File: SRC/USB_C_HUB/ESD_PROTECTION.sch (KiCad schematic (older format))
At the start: 3 parts

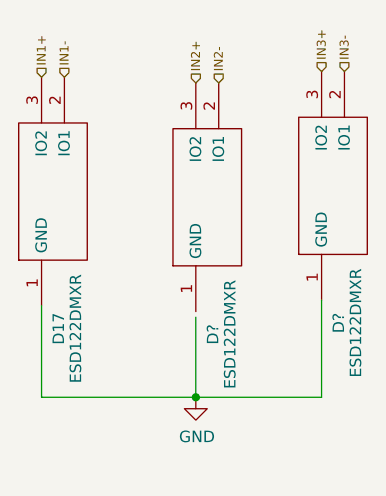
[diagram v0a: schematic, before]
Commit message: schematic capture complete. Pending Footprint assignment. accetable Errors=21
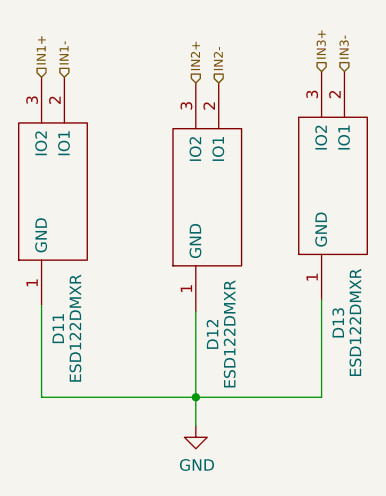
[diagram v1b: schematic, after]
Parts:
- gave numbers to parts that had none: 2
- renumbered D17 to D11
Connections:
- wire segments 5 -> 6
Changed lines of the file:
@@
 $Descr A4 11693 8268
 encoding utf-8
-Sheet 9 15
+Sheet 5 15
 Title ""
 Date ""
@@
 P 4275 4300
 AR Path="/62E89C00" Ref="D?"  Part="1"
-AR Path="/62E5065E/62E89C00" Ref="D17"  Part="1"
+AR Path="/62E5065E/62E89C00" Ref="D11"  Part="1"
 AR Path="/6317BD10/62E89C00" Ref="D20"  Part="1"
-AR Path="/63404DD9/62E89C00" Ref="D18"  Part="1"
-AR Path="/639E17BA/62E89C00" Ref="D19"  Part="1"
-F 0 "D17" H 4175 4225 50  0000 C CNN
+AR Path="/63404DD9/62E89C00" Ref="D14"  Part="1"
+AR Path="/639E17BA/62E89C00" Ref="D17"  Part="1"
+F 0 "D11" H 4175 4225 50  0000 C CNN
 F 1 "ESD122DMXR" H 4175 4150 50  0000 C CNN
 F 2 "SamacSys_Parts_2:DMX0003A" H 5125 4400 50  0001 L CNN
@@
 IN1-
 $Comp
-L OLIMEX_Power:GND #PWR0200
+L OLIMEX_Power:GND #PWR073
 U 1 1 630FD5DF
-P 4950 4700
-AR Path="/62E5065E/630FD5DF" Ref="#PWR0200"  Part="1"
-AR Path="/6317BD10/630FD5DF" Ref="#PWR0203"  Part="1"
-AR Path="/63404DD9/630FD5DF" Ref="#PWR0201"  Part="1"
-AR Path="/639E17BA/630FD5DF" Ref="#PWR0202"  Part="1"
-F 0 "#PWR0200" H 4950 4450 50  0001 C CNN
-F 1 "GND" H 4955 4527 50  0000 C CNN
-F 2 "" H 4950 4700 60  0000 C CNN
-F 3 "" H 4950 4700 60  0000 C CNN
-	1    4950 4700
+P 4950 4825
+AR Path="/62E5065E/630FD5DF" Ref="#PWR073"  Part="1"
+AR Path="/6317BD10/630FD5DF" Ref="#PWR076"  Part="1"
+AR Path="/63404DD9/630FD5DF" Ref="#PWR074"  Part="1"
+AR Path="/639E17BA/630FD5DF" Ref="#PWR075"  Part="1"
+F 0 "#PWR073" H 4950 4575 50  0001 C CNN
+F 1 "GND" H 4955 4652 50  0000 C CNN
+F 2 "" H 4950 4825 60  0000 C CNN
+F 3 "" H 4950 4825 60  0000 C CNN
+	1    4950 4825
 	1    0    0    -1
 $EndComp
@@
 P 4950 4325
 AR Path="/642DE3EE" Ref="D?"  Part="1"
-AR Path="/62E5065E/642DE3EE" Ref="D?"  Part="1"
-AR Path="/6317BD10/642DE3EE" Ref="D?"  Part="1"
-AR Path="/63404DD9/642DE3EE" Ref="D?"  Part="1"
-AR Path="/639E17BA/642DE3EE" Ref="D?"  Part="1"
-F 0 "D?" H 4850 4250 50  0000 C CNN
+AR Path="/62E5065E/642DE3EE" Ref="D12"  Part="1"
+AR Path="/6317BD10/642DE3EE" Ref="D21"  Part="1"
+AR Path="/63404DD9/642DE3EE" Ref="D15"  Part="1"
+AR Path="/639E17BA/642DE3EE" Ref="D18"  Part="1"
+F 0 "D12" H 4850 4250 50  0000 C CNN
 F 1 "ESD122DMXR" H 4850 4175 50  0000 C CNN
 F 2 "SamacSys_Parts_2:DMX0003A" H 5800 4425 50  0001 L CNN
@@
 P 5500 4275
 AR Path="/642DE7EE" Ref="D?"  Part="1"
-AR Path="/62E5065E/642DE7EE" Ref="D?"  Part="1"
-AR Path="/6317BD10/642DE7EE" Ref="D?"  Part="1"
-AR Path="/63404DD9/642DE7EE" Ref="D?"  Part="1"
-AR Path="/639E17BA/642DE7EE" Ref="D?"  Part="1"
-F 0 "D?" H 5400 4200 50  0000 C CNN
+AR Path="/62E5065E/642DE7EE" Ref="D13"  Part="1"
+AR Path="/6317BD10/642DE7EE" Ref="D22"  Part="1"
+AR Path="/63404DD9/642DE7EE" Ref="D16"  Part="1"
+AR Path="/639E17BA/642DE7EE" Ref="D19"  Part="1"
+F 0 "D13" H 5400 4200 50  0000 C CNN
 F 1 "ESD122DMXR" H 5400 4125 50  0000 C CNN
 F 2 "SamacSys_Parts_2:DMX0003A" H 6350 4375 50  0001 L CNN
@@
 Wire Wire Line
 	4275 4700 4950 4700
+Wire Wire Line
+	4950 4325 4950 4700
 Connection ~ 4950 4700
 Wire Wire Line
 	4950 4700 5500 4700
 Wire Wire Line
-	4950 4350 4950 4700
+	4950 4825 4950 4700
 $EndSCHEMATC

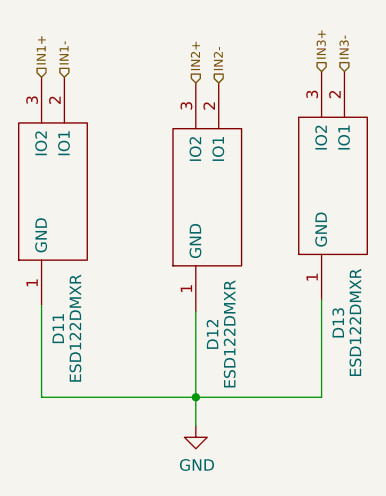
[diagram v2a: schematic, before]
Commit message: schematic capture and footprint assignment complete. Pending approval
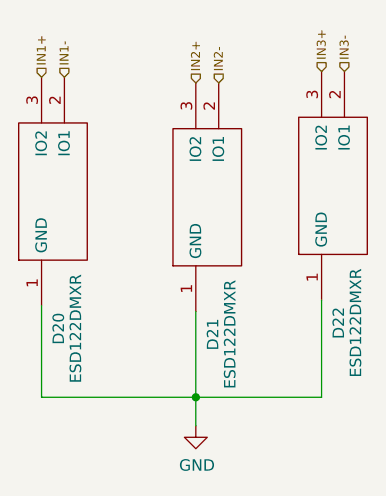
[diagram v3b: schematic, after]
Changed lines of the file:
@@
 $Descr A4 11693 8268
 encoding utf-8
-Sheet 5 15
+Sheet 7 15
 Title "USB C HUB"
 Date "2021-10-28"
@@
 AR Path="/63404DD9/62E89C00" Ref="D14"  Part="1"
 AR Path="/639E17BA/62E89C00" Ref="D17"  Part="1"
-F 0 "D11" H 4175 4225 50  0000 C CNN
+F 0 "D20" H 4175 4225 50  0000 C CNN
 F 1 "ESD122DMXR" H 4175 4150 50  0000 C CNN
 F 2 "SamacSys_Parts_2:DMX0003A" H 5125 4400 50  0001 L CNN
@@
 AR Path="/63404DD9/630FD5DF" Ref="#PWR074"  Part="1"
 AR Path="/639E17BA/630FD5DF" Ref="#PWR075"  Part="1"
-F 0 "#PWR073" H 4950 4575 50  0001 C CNN
+F 0 "#PWR076" H 4950 4575 50  0001 C CNN
 F 1 "GND" H 4955 4652 50  0000 C CNN
 F 2 "" H 4950 4825 60  0000 C CNN
@@
 AR Path="/63404DD9/642DE3EE" Ref="D15"  Part="1"
 AR Path="/639E17BA/642DE3EE" Ref="D18"  Part="1"
-F 0 "D12" H 4850 4250 50  0000 C CNN
+F 0 "D21" H 4850 4250 50  0000 C CNN
 F 1 "ESD122DMXR" H 4850 4175 50  0000 C CNN
 F 2 "SamacSys_Parts_2:DMX0003A" H 5800 4425 50  0001 L CNN
@@
 AR Path="/63404DD9/642DE7EE" Ref="D16"  Part="1"
 AR Path="/639E17BA/642DE7EE" Ref="D19"  Part="1"
-F 0 "D13" H 5400 4200 50  0000 C CNN
+F 0 "D22" H 5400 4200 50  0000 C CNN
 F 1 "ESD122DMXR" H 5400 4125 50  0000 C CNN
 F 2 "SamacSys_Parts_2:DMX0003A" H 6350 4375 50  0001 L CNN
